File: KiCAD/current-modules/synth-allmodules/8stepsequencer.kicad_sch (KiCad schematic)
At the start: 0 parts

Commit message: Sequencer Start
Additions:
- Added all components for sequencer schematic
Changes:
- None
Removals:
- None
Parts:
- added C4: C, symbol Device:C
- added C5: C_Polarized, symbol Device:C_Polarized
- added D7: 1N4148, Diode_THT:D_DO-35_SOD27_P7.62mm_Horizontal, symbol Diode:1N4148
- added D8: LED, symbol Device:LED
- added R19: R, symbol Device:R
- added RV6: R_Potentiometer, symbol Device:R_Potentiometer
- added SW2: SW_Rotary_1x12, symbol Switch:SW_Rotary_1x12
- added SW3: SW_Push, symbol Switch:SW_Push
- added SW4: SW_SPDT, symbol Switch:SW_SPDT
- added SW5: SW_SPST, symbol Switch:SW_SPST
- added U3: CD4017BEE4, CD4017BEE4:DIP794W45P254L1969H508Q16, symbol CD4017BEE4:CD4017BEE4
- added U4: CD40106BEE4, CD40106BEE4:DIP794W45P254L1969H508Q14, symbol Library:CD40106BEE4
- added U5: TL072, symbol Amplifier_Operational:TL072
- added U6: L7808, symbol Regulator_Linear:L7808

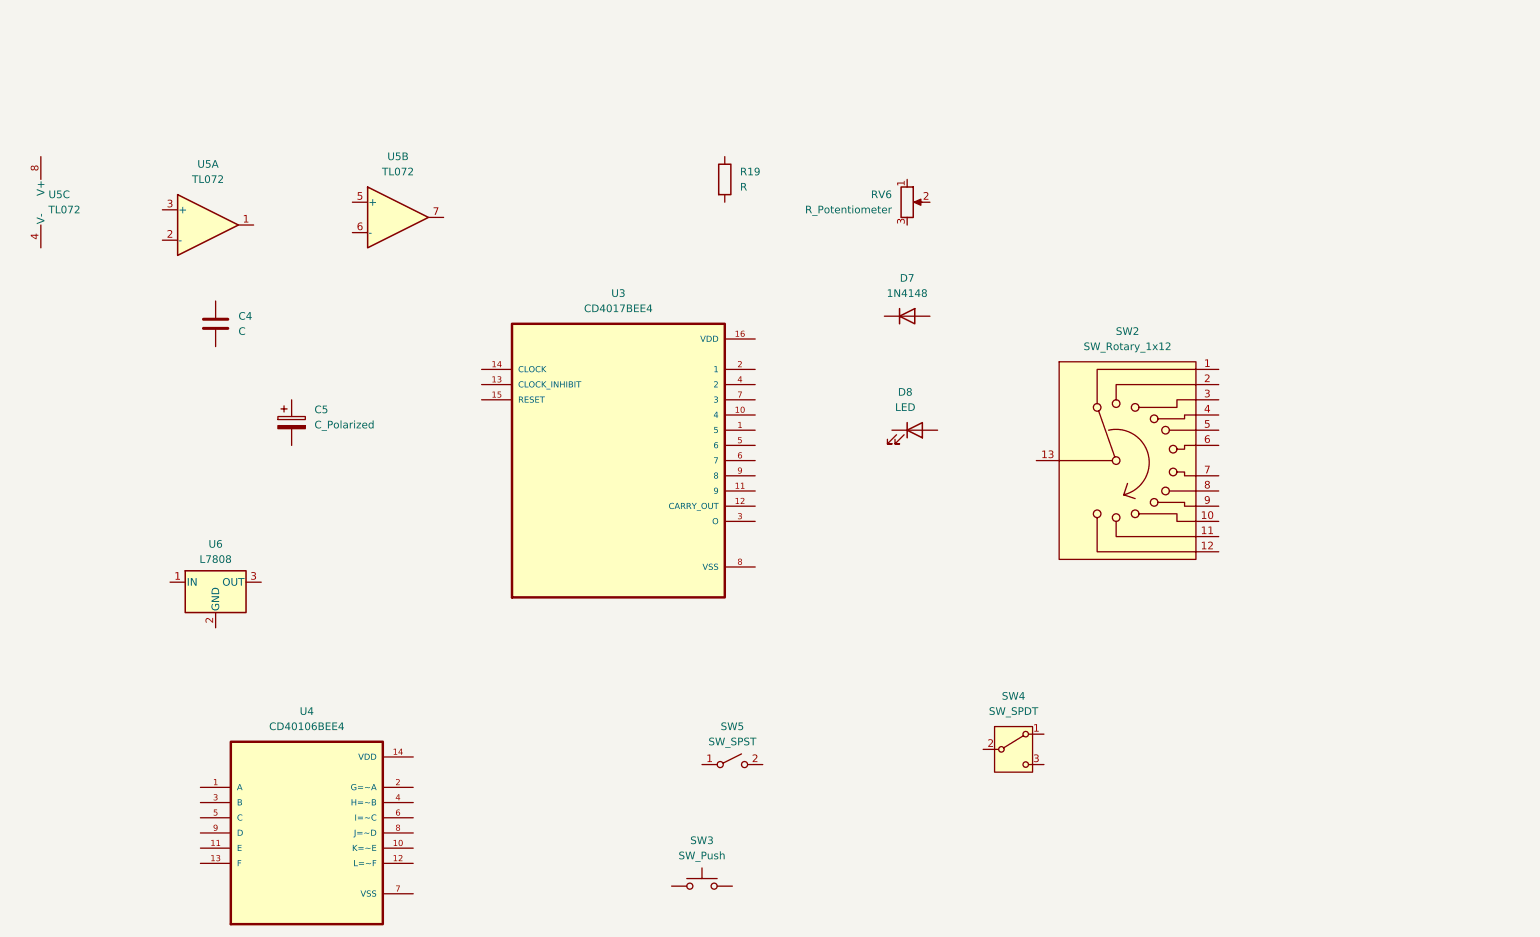
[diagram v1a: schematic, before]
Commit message: Mostly Finished Sequencer
Additions:
- Wired up sequencer except for IOs
Changes:
- None
Removals:
- None
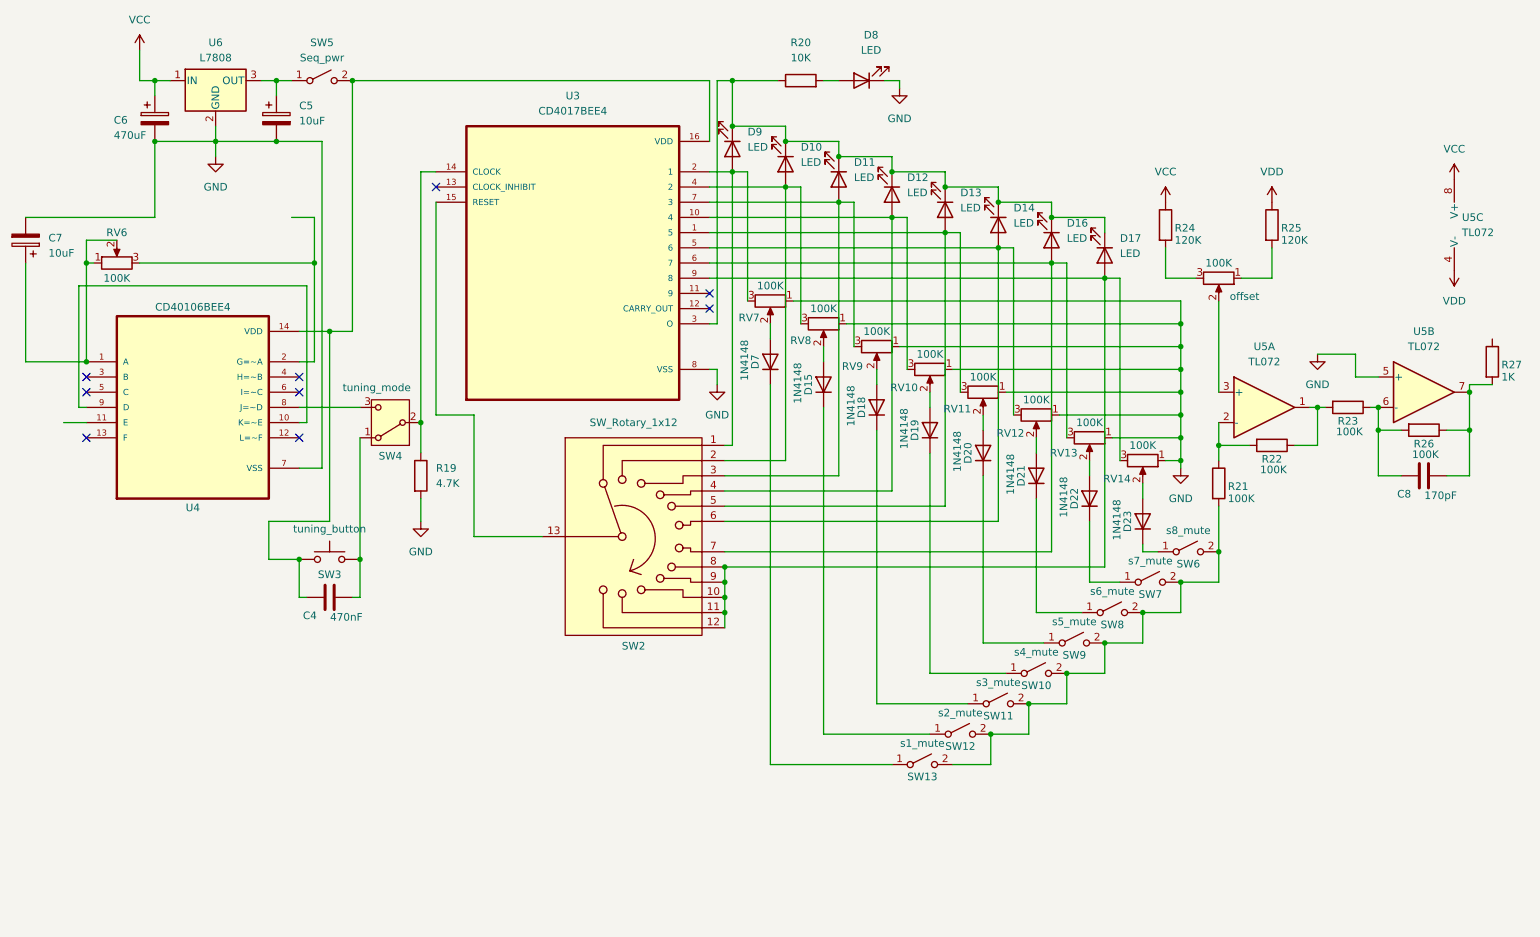
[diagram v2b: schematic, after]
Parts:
- added C6: 470uF, symbol Device:C_Polarized
- added C7: 10uF, symbol Device:C_Polarized
- added C8: 170pF, symbol Device:C
- added D10, D11, D12, D13, D14, D16, D17, D9: LED, symbol Device:LED
- added D15, D18, D19, D20, D21, D22, D23: 1N4148, Diode_THT:D_DO-35_SOD27_P7.62mm_Horizontal, symbol Diode:1N4148
- added R20: 10K, symbol Device:R
- added R21, R22, R23, R26: 100K, symbol Device:R
- added R24, R25: 120K, symbol Device:R
- added R27: 1K, symbol Device:R
- added RV10, RV11, RV12, RV13, RV14, RV7, RV8, RV9, offset: 100K, symbol Device:R_Potentiometer
- added SW10: s4_mute, symbol Switch:SW_SPST
- added SW11: s3_mute, symbol Switch:SW_SPST
- added SW12: s2_mute, symbol Switch:SW_SPST
- added SW13: s1_mute, symbol Switch:SW_SPST
- added SW6: s8_mute, symbol Switch:SW_SPST
- added SW7: s7_mute, symbol Switch:SW_SPST
- added SW8: s6_mute, symbol Switch:SW_SPST
- added SW9: s5_mute, symbol Switch:SW_SPST
- C4: value C -> 470nF
- C5: value C_Polarized -> 10uF
- R19: value R -> 4.7K
- RV6: value R_Potentiometer -> 100K
- SW3: value SW_Push -> tuning_button
- SW4: value SW_SPDT -> tuning_mode
- SW5: value SW_SPST -> Seq_pwr
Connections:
- net at C4.1: now also SW3.1, SW5.2 (B), U3.16 (VDD), U4.14 (VDD)
- net at C4.2: now also SW3.2, SW4.1 (A)
- net at SW4.2 (B): now also R19.1, U3.14 (CLOCK)
- net at SW4.3 (C): now also U4.8 (J=~D)
- net VDD: now reaches U5.4 (V-)
- net VDD: now also R25.1
- net VCC: now reaches U5.8 (V+)
- net VCC: now also U6.1 (IN), C6.1, R24.1
- net GND: now reaches U6.2 (GND)
- net GND: now also C5.2, D8.1 (K), R19.2, U3.8 (VSS), U4.7 (VSS), U5.5 (+), C6.2, C7.2, RV10.1, RV11.1, RV12.1, RV13.1, RV14.1, RV7.1, RV8.1, RV9.1
- net at U6.3 (OUT): now also C5.1, SW5.1 (A)
- net at U5.1: now also R22.1, R23.2
- net at U5.2 (-): now also R21.1, R22.2
- net at U5.3 (+): now also offset.2
- net at D8.2 (A): now also R20.2
- net at U5.6 (-): now also C8.1, R23.1, R26.2
- net at U5.7: now also C8.2, R26.1, R27.2
- net at U4.1 (A): now also RV6.1, RV6.2, C7.1
- net at U4.10 (K=~E): now also U4.9 (D)
- net at U4.2 (G=~A): now also RV6.3
- net at SW2.1: now also U3.2 (1), D9.2 (A), RV7.3
- net at SW2.10: now also SW2.11, SW2.12, SW2.8, SW2.9, U3.9 (8), D17.2 (A), RV14.3
- net at SW2.13: now also U3.15 (RESET)
- net at SW2.2: now also U3.4 (2), D10.2 (A), RV8.3
- net at SW2.3: now also U3.7 (3), D11.2 (A), RV9.3
- net at SW2.4: now also U3.10 (4), D12.2 (A), RV10.3
- net at SW2.5: now also U3.1 (5), D13.2 (A), RV11.3
- net at SW2.6: now also U3.5 (6), D14.2 (A), RV12.3
- net at SW2.7: now also U3.6 (7), D16.2 (A), RV13.3
- net at U3.3 (O): now also D10.1 (K), D11.1 (K), D12.1 (K), D13.1 (K), D14.1 (K), D16.1 (K), D17.1 (K), D9.1 (K), R20.1
- net at D7.1 (K): now also SW13.1 (A)
- net at D7.2 (A): now also RV7.2
- new net: D18.1 (K), SW11.1 (A)
- new net: R21.2, SW10.2 (B), SW11.2 (B), SW12.2 (B), SW13.2 (B), SW6.2 (B), SW7.2 (B), SW8.2 (B), SW9.2 (B)
- new net: R24.2, offset.3
- new net: D22.2 (A), RV13.2
- new net: D19.1 (K), SW10.1 (A)
- new net: D19.2 (A), RV10.2
- new net: D20.2 (A), RV11.2
- new net: D21.1 (K), SW8.1 (A)
- new net: D20.1 (K), SW9.1 (A)
- new net: D23.1 (K), SW6.1 (A)
- new net: D23.2 (A), RV14.2
- new net: D22.1 (K), SW7.1 (A)
- new net: D21.2 (A), RV12.2
- new net: D18.2 (A), RV9.2
- new net: R25.2, offset.1
- new net: D15.1 (K), SW12.1 (A)
- new net: D15.2 (A), RV8.2
- no-connect marks 0 -> 9
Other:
- moved on the sheet: C4, C5, D7, D8, R19, RV6, SW2, SW3, SW4, SW5, U3, U4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
